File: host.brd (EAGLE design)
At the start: 82.5 x 43.3 mm, 25 parts, among them IC10 74LVC1T45W6-7, IC11 74LVC1T45W6-7, IC12 74LVC1T45W6-7, IC2 NCP187AMT120TAG, IC3 LD39200PU33R, IC8 74LVC1T45W6-7, Y1 DSC6001J

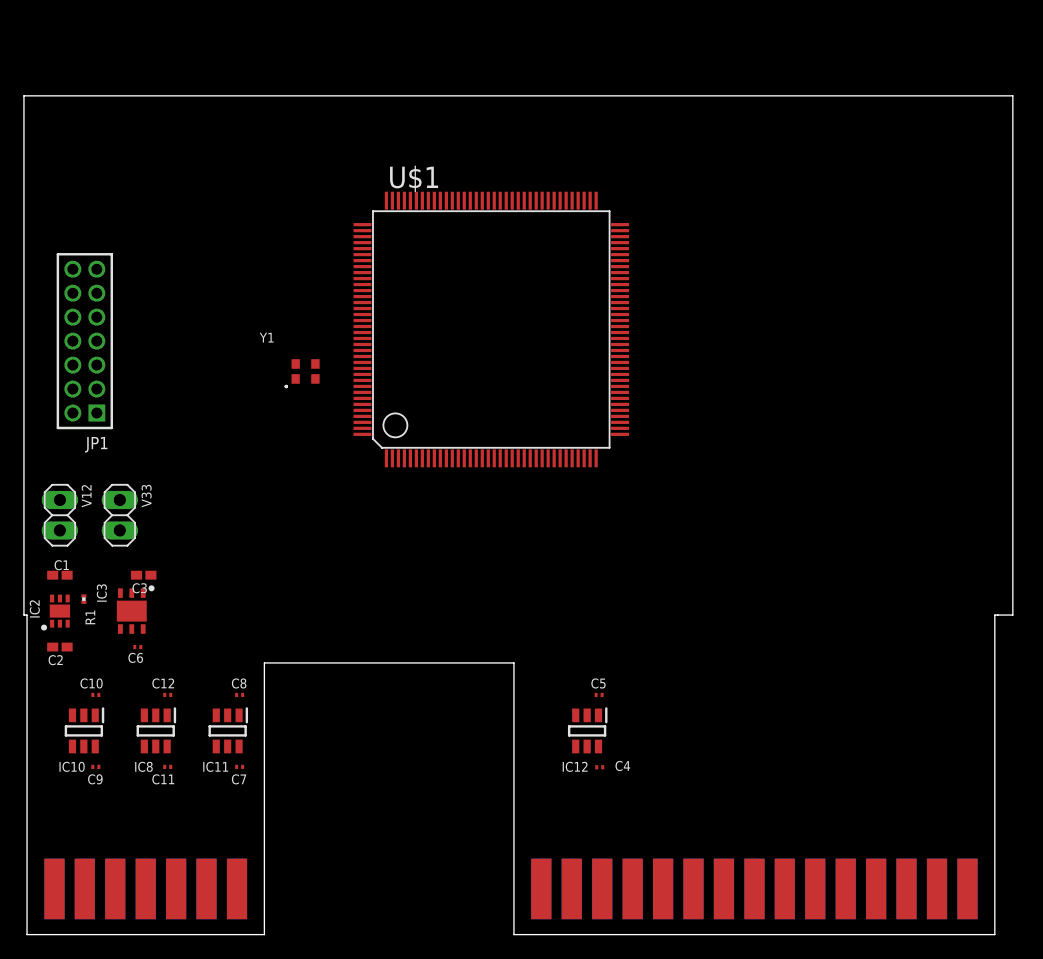
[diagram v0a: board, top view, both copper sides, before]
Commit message: Add the level changes (mostly, still need decoupling and connection to FPGA)
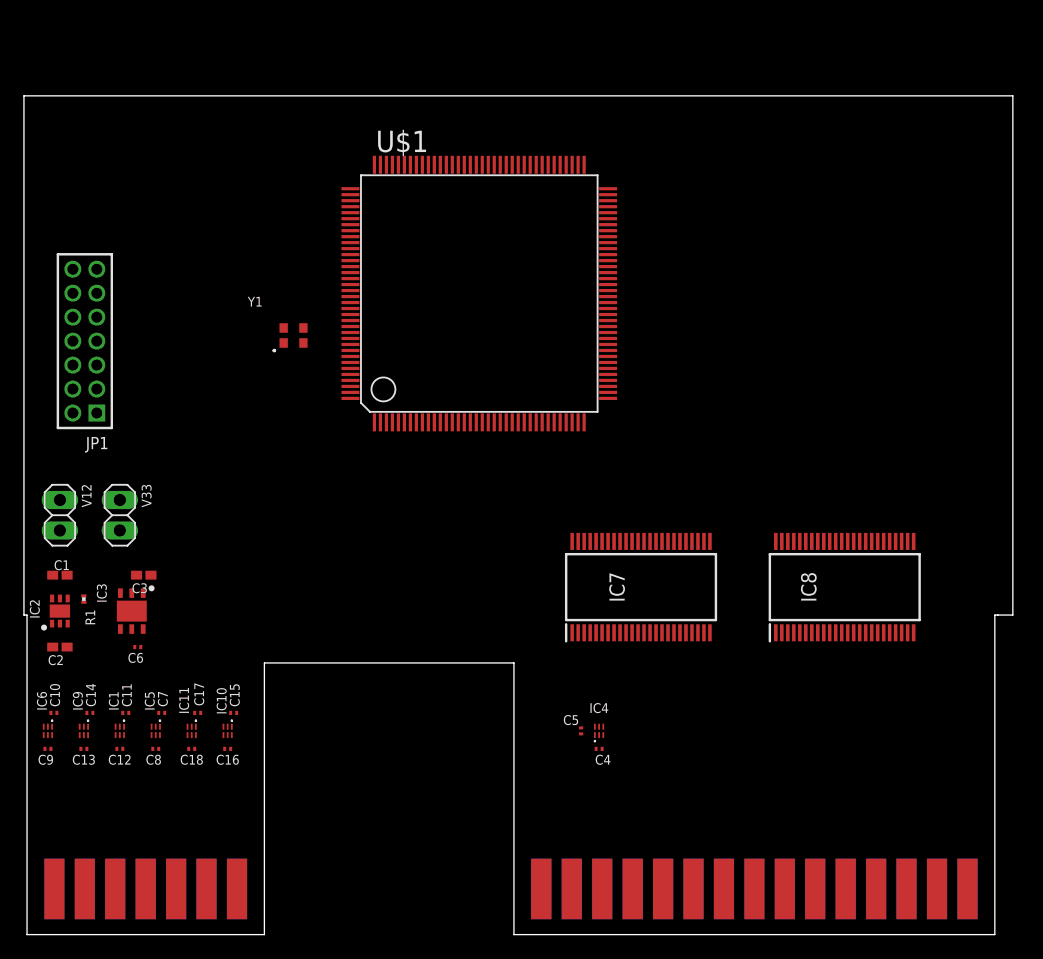
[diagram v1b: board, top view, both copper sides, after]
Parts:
- removed IC12: 74LVC1T45W6-7, samacsys:SOT95P285X140-6N
- added C13, C14, C15, C16, C17, C18: 100nF, rcl:C0201
- added IC1, IC4, IC5, IC6, IC9: 74LVC1T45GS,132, host:74LVC1G3157GS132
- added IC7: 74ALVC164245DGG:11, samacsys:SOP50P810X120-48N
- IC10, IC11: value 74LVC1T45W6-7 -> 74LVC1T45GS,132; device samacsys:SOT95P285X140-6N -> host:74LVC1G3157GS132
- IC8: value 74LVC1T45W6-7 -> 74ALVC164245DGG:11; device samacsys:SOT95P285X140-6N -> samacsys:SOP50P810X120-48N
- moved IC8 58.7 mm to (68.5, 29.0), turned to 90 degrees
- moved IC10 12.0 mm to (17.0, 17.0), turned to 180 degrees
- moved C8 8.32 mm to (11.0, 15.5)
- moved C7 7.91 mm to (11.5, 18.5)
- moved C12 6.02 mm to (8.00, 15.5), turned to 0 degrees
- moved C11 5.70 mm to (8.50, 18.5), turned to 0 degrees
- moved C9 4.27 mm to (2.00, 15.5)
- moved C10 3.81 mm to (2.50, 18.5)
- moved C5 3.35 mm to (46.5, 17.0), turned to 90 degrees
- moved U$1 3.16 mm to (38.0, 53.5)
- moved Y1 3.16 mm to (22.5, 50.0)
- moved IC11 3.00 mm to (14.0, 17.0), turned to 180 degrees
- moved C4 1.53 mm to (48.0, 15.5), turned to 0 degrees
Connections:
- new net !EXTSEL!: IC10.3
- new net !IRQ!: IC11.3
- new net !MPD!: IC9.3
- new net DIR_EXTSEL: IC10.5
- new net DIR_IRQ: IC11.5
- new net DIR_MPD: IC9.5
- net !A8_CCTL!: now also IC7.3
- net !A8_CLK!: now also IC7.5
- net !A8_D1XX!: now also IC7.2
- net !A8_EXTSEL!: now also IC10.4
- net !A8_HALT!: now also IC1.4; no longer IC8.4
- net !A8_IRQ!: now also IC11.4
- net !A8_MPD!: now also IC9.4
- net !A8_REF!: now also IC6.4; no longer IC10.4
- net !A8_RESET!: now also IC5.4; no longer IC11.4
- net !A8_S4!: now also IC7.9
- net !A8_S5!: now also IC7.8
- net !HALT!: now also IC1.3; no longer IC8.3
- net !REF!: now also IC6.3; no longer IC10.3
- net !RESET!: now also IC5.3; no longer IC11.3
- net +3V3: now also C14.1, C16.1, C18.1, IC1.1, IC4.1, IC5.1, IC6.1, IC9.1; no longer IC12.1, IC8.1
- net +5V: now also C13.1, C15.1, C17.1, IC1.6, IC4.6, IC5.6, IC6.6, IC9.6; no longer IC12.6, IC8.6
- net A8_A0: now also IC8.16
- net A8_A1: now also IC8.19
- net A8_A10: now also IC8.6
- net A8_A11: now also IC8.8
- net A8_A12: now also IC8.9
- net A8_A13: now also IC8.5
- net A8_A14: now also IC8.3
- net A8_A15: now also IC8.2
- net A8_A2: now also IC8.22
- net A8_A3: now also IC8.23
- net A8_A4: now also IC8.20
- net A8_A5: now also IC8.17
- net A8_A6: now also IC8.14
- net A8_A7: now also IC8.13
- net A8_A8: now also IC8.12
- net A8_A9: now also IC8.11
- net A8_D0: now also IC7.17
- net A8_D1: now also IC7.19
- net A8_D2: now also IC7.20
- net A8_D3: now also IC7.16
- net A8_D4: now also IC7.23
- net A8_D5: now also IC7.22
- net A8_D6: now also IC7.14
- net A8_D7: now also IC7.13
- net A8_R/!W!: now also IC4.4; no longer IC12.4
- net A8_RD4: now also IC7.11
- net A8_RD5: now also IC7.6
- net DIR_HALT: now also IC1.5; no longer IC8.5
- net DIR_REF: now also IC6.5; no longer IC10.5
- net DIR_RST: now also IC5.5; no longer IC11.5
- net DIR_RW: now also IC4.5; no longer IC12.5
- net GND: now also IC4.2, IC5.2, IC6.2; no longer IC10.2, IC11.2, IC12.2, IC8.2
- net GND1: now also C13.2, C14.2, C15.2, C16.2, C17.2, C18.2, IC1.2, IC10.2, IC11.2, IC9.2
- net R/!W!: now also IC4.3; no longer IC12.3

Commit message: Move to 6-layer board for supply cleanliness
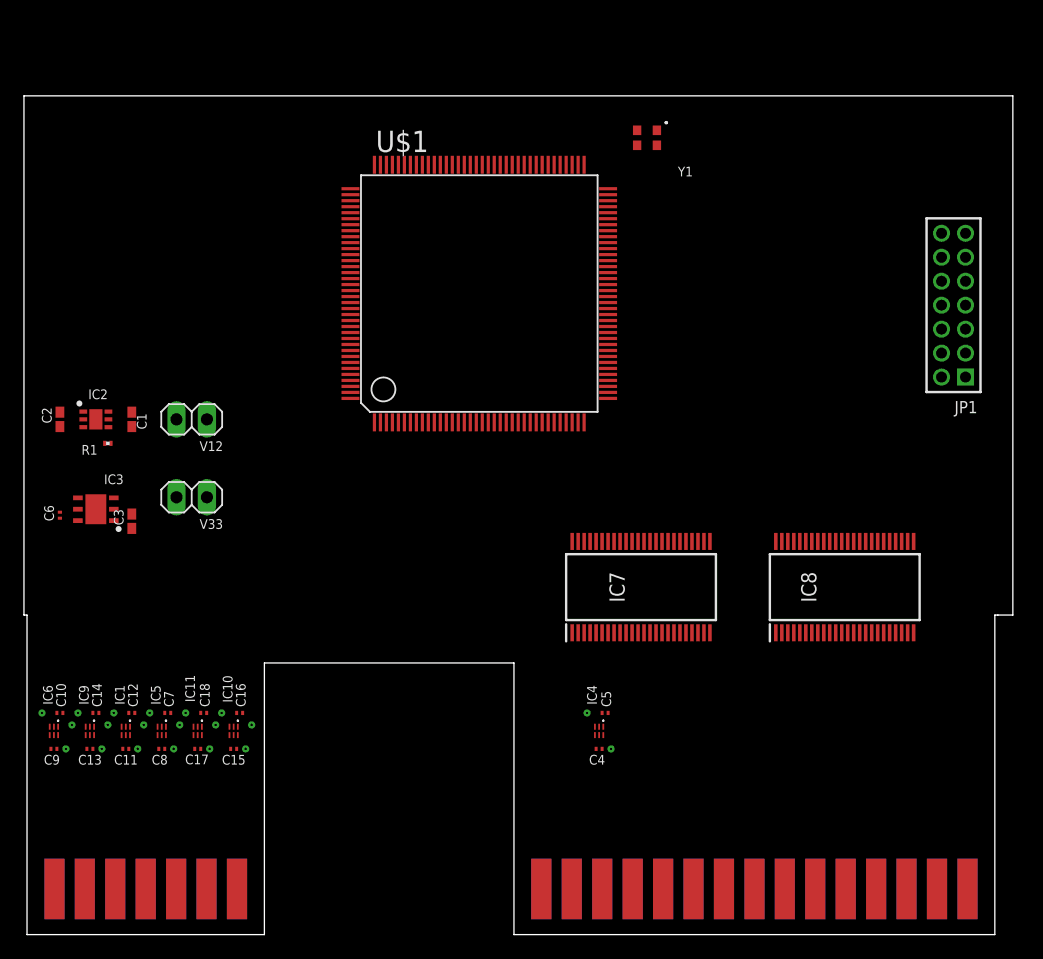
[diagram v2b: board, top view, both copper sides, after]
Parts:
- moved JP1 72.6 mm to (77.6, 52.5)
- moved Y1 33.8 mm to (52.0, 66.5), turned to 180 degrees
- moved C2 19.0 mm to (3.00, 43.0), turned to 270 degrees
- moved IC2 16.3 mm to (6.00, 43.0), turned to 0 degrees
- moved C1 14.3 mm to (9.00, 43.0), turned to 270 degrees
- moved V12 13.6 mm to (14.0, 43.0), turned to 180 degrees
- moved R1 13.2 mm to (7.00, 41.0), turned to 180 degrees
- moved C6 12.8 mm to (3.00, 35.0), turned to 90 degrees
- moved IC3 9.01 mm to (6.00, 35.5), turned to 180 degrees
- moved V33 6.18 mm to (14.0, 36.5), turned to 180 degrees
- moved C3 4.61 mm to (9.00, 34.5), turned to 270 degrees
- moved C12 3.16 mm to (9.00, 18.5), turned to 180 degrees
- moved C16 3.16 mm to (18.0, 18.5)
- moved C18 3.16 mm to (15.0, 18.5)
- moved C11 3.00 mm to (8.50, 15.5), turned to 180 degrees
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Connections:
- removed net GND1: C11.2, C12.2, C13.2, C14.2, C15.2, C16.2, C17.2, C18.2, IC1.2, IC10.2, IC11.2, IC9.2
- net +1.2V: now also U$1.107, U$1.125, U$1.128, U$1.13, U$1.130, U$1.2, U$1.22, U$1.49, U$1.57, U$1.73, U$1.85, U$1.96
- net +5V: now also IC7.18, IC7.7, IC8.18, IC8.7
- net CLK25: now also U$1.75; no longer U$1.132
- net GND: now also C11.2, C12.2, C13.2, C14.2, C15.2, C16.2, C17.2, C18.2, IC1.2, IC10.2, IC11.2, IC9.2
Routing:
- added copper zone on layer 3, net +1.2V
- added copper zone on layer 2, net +3V3
- added copper zone on layer 2, net +5V
- added copper zone on layer 15, net GND

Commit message: Hook up the level-translators to the FPGA
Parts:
- moved Y1 19.0 mm to (33.0, 66.5), turned to 0 degrees
- moved U$1 10.0 mm to (48.0, 53.5), turned to 90 degrees
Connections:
- new net !CCTL!: IC7.46, U$1.111
- new net !D1XX!: IC7.47, U$1.112
- new net !S4!: IC7.40, U$1.118
- new net !S5!: IC7.41, U$1.117
- new net A0: IC8.33, U$1.11
- new net A1: IC8.30, U$1.15
- new net A10: IC8.43, U$1.144
- new net A11: IC8.41, U$1.3
- new net A12: IC8.40, U$1.4
- new net A13: IC8.44, U$1.142
- new net A14: IC8.46, U$1.141
- new net A15: IC8.47, U$1.140
- new net A2: IC8.27, U$1.17
- new net A3: IC8.26, U$1.18
- new net A4: IC8.29, U$1.16
- new net A5: IC8.32, U$1.14
- new net A6: IC8.35, U$1.10
- new net A7: IC8.36, U$1.8
- new net A8: IC8.37, U$1.7
- new net A9: IC8.38, U$1.6
- new net CLK: IC7.44, U$1.113
- new net D0: IC7.32, U$1.132
- new net D1: IC7.30, U$1.134
- new net D2: IC7.29, U$1.135
- new net D3: IC7.33, U$1.131
- new net D4: IC7.26, U$1.137
- new net D5: IC7.27, U$1.136
- new net D6: IC7.35, U$1.124
- new net D7: IC7.36, U$1.123
- new net DIR_A: IC8.1, IC8.24, U$1.139
- new net DIR_D: IC7.24, U$1.138
- new net DIR_IN: IC7.1, U$1.110
- new net RD4: IC7.38, U$1.119
- new net RD5: IC7.43, U$1.114
- net !EXTSEL!: now also U$1.106
- net !HALT!: now also U$1.99
- net !IRQ!: now also U$1.103
- net !MPD!: now also U$1.97
- net !REF!: now also U$1.92
- net !RESET!: now also U$1.101
- net +3V3: now also U$1.12, U$1.122, U$1.143, U$1.21, U$1.88, U$1.91, U$1.95
- net DIR_EXTSEL: now also U$1.109
- net DIR_HALT: now also U$1.100
- net DIR_IRQ: now also U$1.105
- net DIR_MPD: now also U$1.98
- net DIR_REF: now also U$1.93
- net DIR_RST: now also U$1.102
- net DIR_RW: now also U$1.116
- net GND: now also IC7.10, IC7.15, IC7.21, IC7.28, IC7.34, IC7.39, IC7.4, IC7.45, IC8.10, IC8.15, IC8.21, IC8.28, IC8.34, IC8.39, IC8.4, IC8.45
- net R/!W!: now also U$1.115

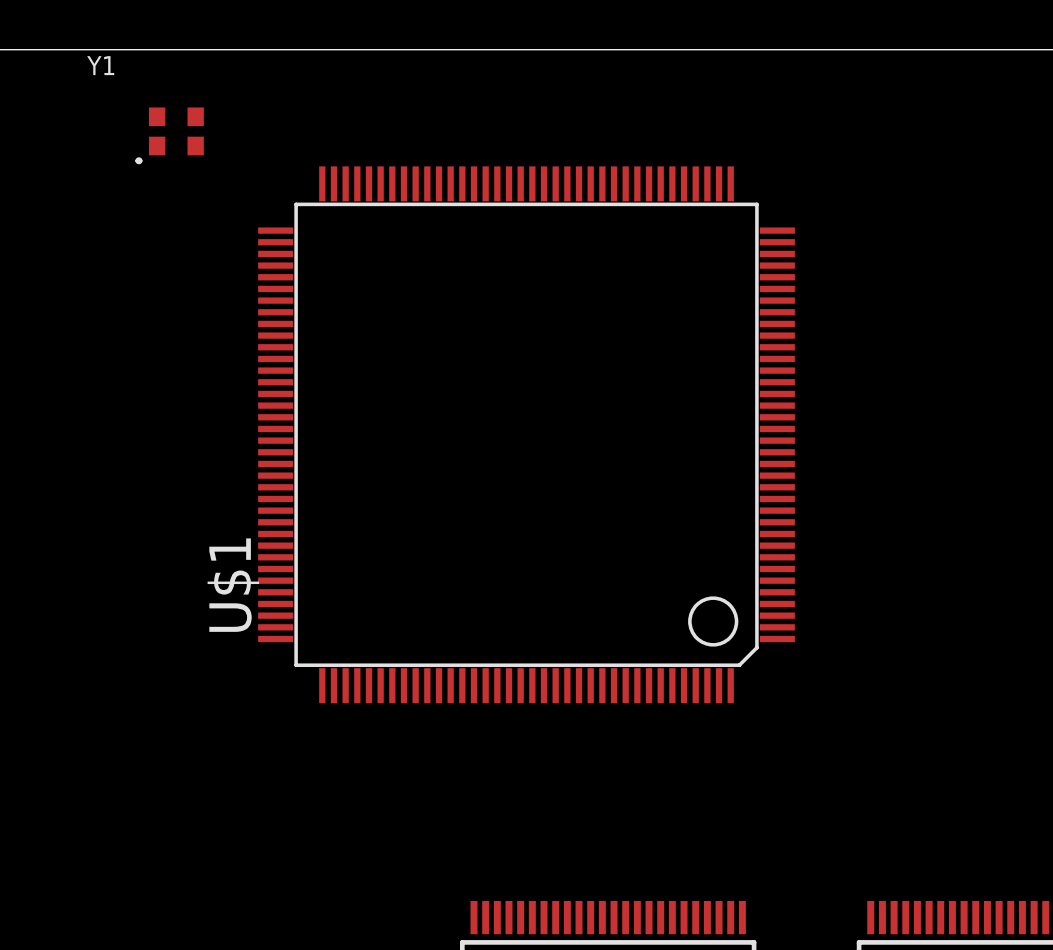
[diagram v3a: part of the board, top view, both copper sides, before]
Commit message: Add FPGA decoupling caps
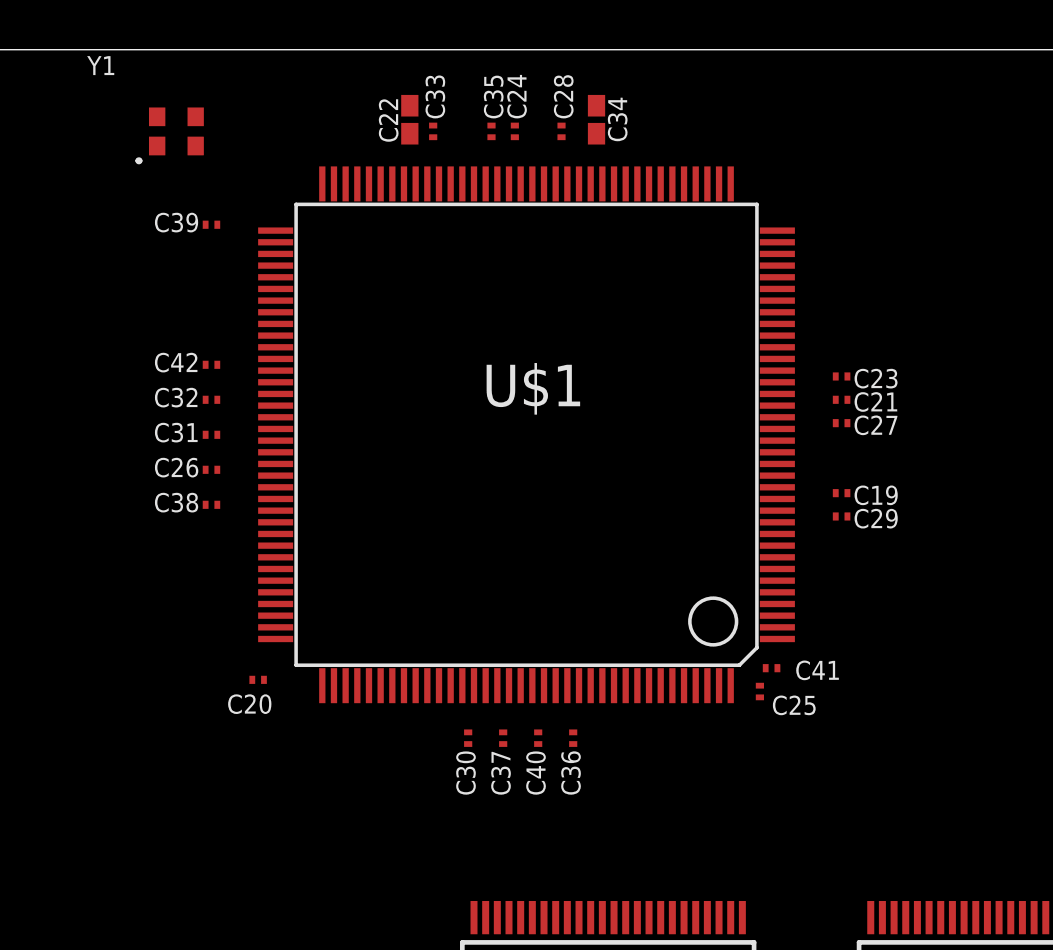
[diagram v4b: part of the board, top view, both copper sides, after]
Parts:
- added C19, C23, C27, C31, C35, C39: 1uF, rcl:C0201
- added C20, C25, C29, C32, C37, C41: 10nF, rcl:C0201
- added C21, C24, C26, C28, C30, C33, C36, C38, C40, C42: 100nF, rcl:C0201
- added C22, C34: 10uF, rcl:C0402K
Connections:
- net +1.2V: now also C19.1, C20.1, C21.1, C34.1, C35.1, C36.1, C37.1, C38.1, C39.1, C40.1, C41.1, C42.1
- net +3V3: now also C22.1, C23.1, C24.1, C25.1, C26.1, C27.1, C28.1, C29.1, C30.1, C31.1, C32.1, C33.1, IC7.31, IC7.42, IC8.31, IC8.42, U$1.23, U$1.51, U$1.52, U$1.62, U$1.63
- net GND: now also C19.2, C20.2, C21.2, C22.2, C23.2, C24.2, C25.2, C26.2, C27.2, C28.2, C29.2, C30.2, C31.2, C32.2, C33.2, C34.2, C35.2, C36.2, C37.2, C38.2, C39.2, C40.2, C41.2, C42.2, IC7.25, IC7.48, IC8.25, IC8.48, U$1.1, U$1.104, U$1.108, U$1.120, U$1.121, U$1.126, U$1.127, U$1.129, U$1.133, U$1.37, U$1.44, U$1.5, U$1.50, U$1.64, U$1.9, U$1.94

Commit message: Add level-translation decoupling caps
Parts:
- added C43, C44, C45, C46, C47, C48, C49, C50: 100nF, rcl:C0201
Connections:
- net +3V3: now also C43.1, C44.1, C45.1, C46.1
- net +5V: now also C47.1, C48.1, C49.1, C50.1
- net GND: now also C43.2, C44.2, C45.2, C46.2, C47.2, C48.2, C49.2, C50.2

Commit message: Working through the design-guide
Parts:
- added C51, C53: 100nF, rcl:C0201
- added C52: 10uF, rcl:C0402K
- added CBSEL0, CBSEL1, CBUS0, CBUS1, CBUS2: (no value), pinhead:1X03
- added FLASH: W25Q32JVSSIQ, SparkFun:SO08
- added R10, R11, R12, R13, R14, R15, R16, R17, R18, R19, R2, R20, R21, R22, R23, R24, R25, R26, R27, R28, R3, R4, R5, R6, R7, R8, R9: 10K, rcl:R0201
- added RESET: (no value), SparkFun:TACTILE-PTH
- added SPV: MIC803-30D2VC3-TR, x-pi:SOT95P237X111-3N
- moved JP1 14.7 mm to (74.5, 66.9), turned to 0 degrees
- moved C19 14.3 mm to (73.0, 42.5)
- moved C20 14.3 mm to (48.0, 34.5)
- moved C21 14.3 mm to (73.0, 46.5)
- moved C22 14.3 mm to (54.5, 58.5)
- moved C23 14.3 mm to (73.0, 47.5)
- moved C24 14.3 mm to (59.0, 58.0)
- moved C25 14.3 mm to (69.5, 34.0)
- moved C26 14.3 mm to (46.0, 43.5)
- moved C27 14.3 mm to (73.0, 45.5)
- moved C28 14.3 mm to (61.0, 58.0)
- moved C29 14.3 mm to (73.0, 41.5)
- moved C30 14.3 mm to (57.0, 32.0)
- moved C31 14.3 mm to (46.0, 45.0)
- moved C32 14.3 mm to (46.0, 46.5)
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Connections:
- new net !CRESET!: C52.1, JP1.5, R9.2, RESET.3, RESET.4, SPV.2, U$1.35
- new net !STATUS!: JP1.6
- new net !TEST!: R5.2, U$1.74
- new net CBSEL0: R23.2, U$1.137
- new net CBSEL1: R24.2, U$1.138
- new net CBUS0: R6.2, U$1.78
- new net CBUS1: R7.2, U$1.79
- new net CBUS2: R8.2, U$1.80
- new net CDONE: JP1.3, R3.2, U$1.34
- new net N$1: CBSEL0.2, R23.1
- new net N$10: CBUS0.2, R6.1
- new net N$11: CBUS1.2, R7.1
- new net N$12: CBUS2.2, R8.1
- new net N$3: CBSEL1.2, R24.1
- new net SPI_CLK: FLASH.6, JP1.13, U$1.30
- new net SPI_CSI: R2.2, U$1.32
- new net SPI_D0: FLASH.5, JP1.11, U$1.29
- new net SPI_D1: FLASH.2, JP1.9, U$1.28
- new net SPI_D2: FLASH.3, U$1.20
- new net SPI_D3: FLASH.7, JP1.1, U$1.19
- new net SPI_SS: FLASH.1, JP1.7, R4.2, U$1.31
- new net TCK: JP1.8, R28.2, U$1.26
- new net TDI: JP1.14, R26.2, U$1.27
- new net TDO: JP1.12, R27.2, U$1.24
- new net TMS: JP1.10, R25.2, U$1.25
- net !CCTL!: now also U$1.109; no longer U$1.111
- net !D1XX!: now also U$1.103; no longer U$1.112
- net !EXTSEL!: now also R22.1, U$1.100; no longer U$1.106
- net !HALT!: now also U$1.93; no longer U$1.99
- net !IRQ!: now also R21.1, U$1.105; no longer U$1.103
- net !MPD!: now also R20.1, U$1.90; no longer U$1.97
- net !REF!: now also U$1.87; no longer U$1.92
- net !RESET!: now also U$1.98; no longer U$1.101
- net !S4!: now also U$1.115; no longer U$1.118
- net !S5!: now also U$1.114; no longer U$1.117
- net +3V3: now also C51.1, C53.1, CBSEL0.1, CBSEL1.1, CBUS0.1, CBUS1.1, CBUS2.1, FLASH.8, R17.2, R18.2, R19.2, R2.1, R20.2, R21.2, R22.2, R25.1, R26.1, R27.1, R28.1, R3.1, R4.1, R5.1, R9.1, SPV.3
- net CLK: now also U$1.110; no longer U$1.113
- net D0: now also U$1.123; no longer U$1.132
- net D1: now also U$1.124; no longer U$1.134
- net D2: now also U$1.131; no longer U$1.135
- net D3: now also U$1.119; no longer U$1.131
- net D4: now also U$1.134; no longer U$1.137
- net D5: now also U$1.132; no longer U$1.136
- net D6: now also U$1.118; no longer U$1.124
- net D7: now also U$1.117; no longer U$1.123
- net DIR_A: now also R10.2
- net DIR_D: now also R11.2, U$1.135; no longer U$1.138
- net DIR_EXTSEL: now also R17.1, U$1.106; no longer U$1.109
- net DIR_HALT: now also R13.2, U$1.97; no longer U$1.100
- net DIR_IN: now also R12.2, U$1.102; no longer U$1.110
- net DIR_IRQ: now also R18.1, U$1.99; no longer U$1.105
- net DIR_MPD: now also R19.1, U$1.92; no longer U$1.98
- net DIR_REF: now also R15.2, U$1.89; no longer U$1.93
- net DIR_RST: now also R14.2, U$1.101; no longer U$1.102
- net DIR_RW: now also R16.2, U$1.113; no longer U$1.116
- net GND: now also C51.2, C52.2, C53.2, CBSEL0.3, CBSEL1.3, CBUS0.3, CBUS1.3, CBUS2.3, FLASH.4, JP1.2, JP1.4, R10.1, R11.1, R12.1, R13.1, R14.1, R15.1, R16.1, RESET.1, RESET.2, SPV.1
- net R/!W!: now also U$1.111; no longer U$1.115
- net RD4: now also U$1.116; no longer U$1.119
- net RD5: now also U$1.112; no longer U$1.114
